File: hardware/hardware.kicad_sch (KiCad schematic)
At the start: 0 parts

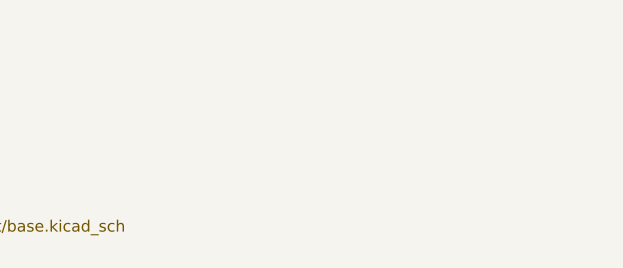
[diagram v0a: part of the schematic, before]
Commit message: add progress on main drive controller and switch to hiearchical labels
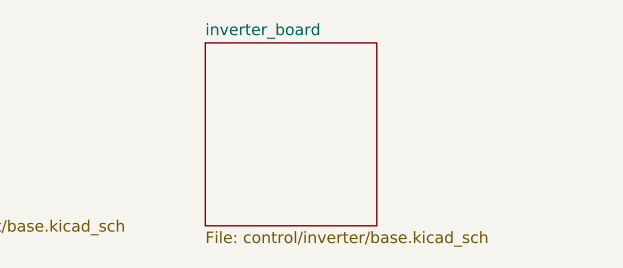
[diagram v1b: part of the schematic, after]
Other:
- added sheet inverter_board (control/inverter/base.kicad_sch)
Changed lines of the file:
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@@
 	(paper "A4")
+	(sheet
+		(at 72.39 41.91)
+		(size 19.05 20.32)
+		(exclude_from_sim no)
+		(in_bom yes)
+		(on_board yes)
+		(dnp no)
+		(fields_autoplaced yes)
+		(stroke
+			(width 0.1524)
+			(type solid)
+		)
+		(fill
+			(color 0 0 0 0.0000)
+		)
+		(property "Sheetname" "inverter_board"
+			(at 72.39 41.1984 0)
+			(effects
+				(font
+					(size 1.27 1.27)
+				)
+				(justify left bottom)
+			)
+		)
+		(property "Sheetfile" "control/inverter/base.kicad_sch"
+			(at 72.39 62.8146 0)
+			(effects
+				(font
+					(size 1.27 1.27)
+				)
+				(justify left top)
+			)
+		)
+		(instances
+			(project "hardware"
+				(path "/606d342f-174b-4504-b335-50f65aa4e733"
+					(page "8")
+				)
+			)
+		)
+	)
 	(sheet
 		(at 35.56 42.545)

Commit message: update
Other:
- added sheet main_coils (power/main_coils/base.kicad_sch)
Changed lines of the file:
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@@
 	(paper "A4")
+	(sheet
+		(at 36.195 168.91)
+		(size 12.7 3.81)
+		(exclude_from_sim no)
+		(in_bom yes)
+		(on_board yes)
+		(dnp no)
+		(fields_autoplaced yes)
+		(stroke
+			(width 0.1524)
+			(type solid)
+		)
+		(fill
+			(color 0 0 0 0.0000)
+		)
+		(property "Sheetname" "main_coils"
+			(at 36.195 168.1984 0)
+			(effects
+				(font
+					(size 1.27 1.27)
+				)
+				(justify left bottom)
+			)
+		)
+		(property "Sheetfile" "power/main_coils/base.kicad_sch"
+			(at 36.195 173.3046 0)
+			(effects
+				(font
+					(size 1.27 1.27)
+				)
+				(justify left top)
+			)
+		)
+		(instances
+			(project "hardware"
+				(path "/606d342f-174b-4504-b335-50f65aa4e733"
+					(page "13")
+				)
+			)
+		)
+	)
 	(sheet
 		(at 72.39 41.91)

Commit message: idk some changes
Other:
- removed sheet main_coils
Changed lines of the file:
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@@
 	(paper "A4")
-	(sheet
-		(at 36.195 168.91)
-		(size 12.7 3.81)
-		(exclude_from_sim no)
-		(in_bom yes)
-		(on_board yes)
-		(dnp no)
-		(fields_autoplaced yes)
-		(stroke
-			(width 0.1524)
-			(type solid)
-		)
-		(fill
-			(color 0 0 0 0.0000)
-		)
-		(property "Sheetname" "main_coils"
-			(at 36.195 168.1984 0)
-			(effects
-				(font
-					(size 1.27 1.27)
-				)
-				(justify left bottom)
-			)
-		)
-		(property "Sheetfile" "power/main_coils/base.kicad_sch"
-			(at 36.195 173.3046 0)
-			(effects
-				(font
-					(size 1.27 1.27)
-				)
-				(justify left top)
-			)
-		)
-		(instances
-			(project "hardware"
-				(path "/606d342f-174b-4504-b335-50f65aa4e733"
-					(page "13")
-				)
-			)
-		)
-	)
 	(sheet
 		(at 72.39 41.91)
